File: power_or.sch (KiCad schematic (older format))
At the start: 25 parts

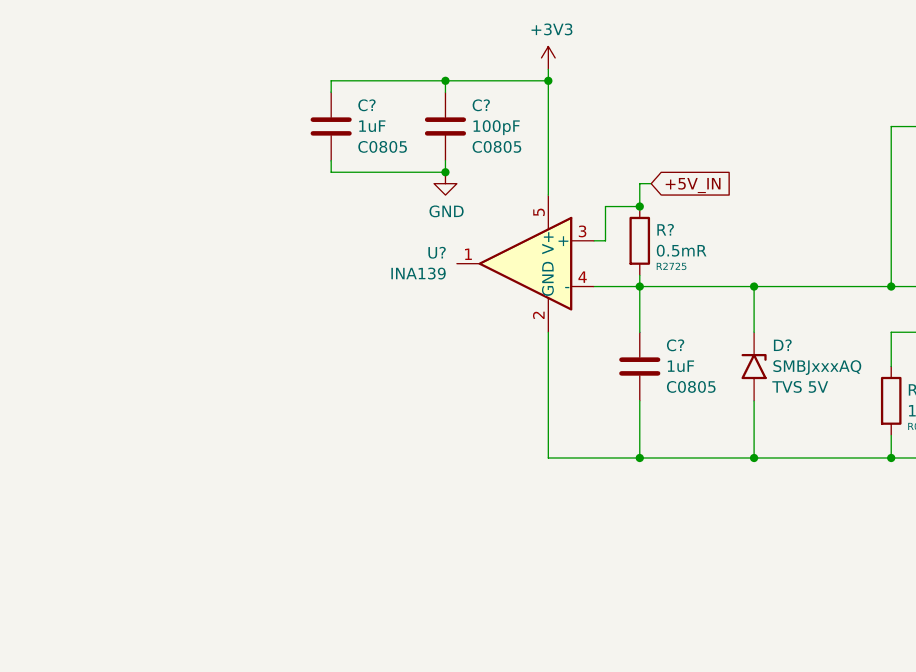
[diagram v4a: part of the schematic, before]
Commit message: move out the current sensor frome power switch
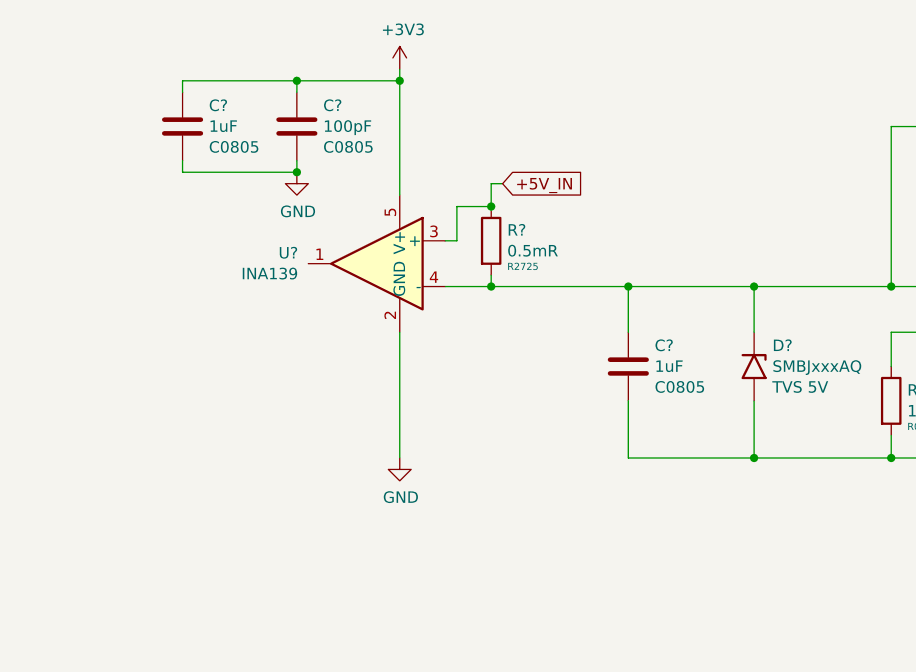
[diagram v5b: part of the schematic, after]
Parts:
- removed C? (x2): 1uF, Capacitor_SMD:C_0805_2012Metric, symbol Device:C
- removed C?: 100pF, Capacitor_SMD:C_0805_2012Metric, symbol Device:C
- removed R?: 0.5mR, Resistor_SMD:R_2725_6865Metric, symbol Device:R
- removed U?: INA139, Package_TO_SOT_SMD:SOT-23-5, symbol Amplifier_Current:INA139
- added C? (x2): 1uF, Capacitor_SMD:C_0805_2012Metric, symbol Device:C
- added C?: 100pF, Capacitor_SMD:C_0805_2012Metric, symbol Device:C
- added R?: 0.5mR, Resistor_SMD:R_2725_6865Metric, symbol Device:R
- added U?: INA139, Package_TO_SOT_SMD:SOT-23-5, symbol Amplifier_Current:INA139
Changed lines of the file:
@@
-$EndComp
-$Comp
-L Amplifier_Current:INA139 U?
-U 1 1 5E3C04AF
-P 6250 1800
-F 0 "U?" H 6594 1846 50  0000 L CNN
-F 1 "INA139" H 6594 1755 50  0000 L CNN
-F 2 "Package_TO_SOT_SMD:SOT-23-5" H 6250 1800 50  0001 C CNN
-F 3 "http://www.ti.com/lit/gpn/ina139" H 6250 1805 50  0001 C CNN
-	1    6250 1800
-	-1   0    0    -1
 $EndComp
 $Comp
@@
 Text GLabel 1400 7300 1    50   Input ~ 0
 +12V_BUS
-Text GLabel 6800 1450 2    50   Input ~ 0
-+5V_IN
 Text GLabel 10600 1750 2    50   Input ~ 0
 +5V_BUS
@@
 	7250 2650 7850 2650
 Connection ~ 7850 2650
-$Comp
-L Device:C C?
-U 1 1 5E3A7B48
-P 6750 2250
-AR Path="/5E350920/5E3A7B48" Ref="C?"  Part="1"
-AR Path="/5E31859C/5E3A7B48" Ref="C?"  Part="1"
-AR Path="/5E3022E2/5E3A7B48" Ref="C?"  Part="1"
-AR Path="/5E3BA3E9/5E3A7B48" Ref="C?"  Part="1"
-F 0 "C?" H 6865 2341 50  0000 L CNN
-F 1 "1uF" H 6865 2250 50  0000 L CNN
-F 2 "Capacitor_SMD:C_0805_2012Metric" H 6788 2100 50  0001 C CNN
-F 3 "~" H 6750 2250 50  0001 C CNN
-F 4 "C0805" H 6865 2159 50  0000 L CNN "size"
-	1    6750 2250
-	1    0    0    -1
-$EndComp
-Wire Wire Line
-	7250 1900 6750 1900
-Wire Wire Line
-	6750 1900 6750 2100
+Wire Wire Line
+	10600 1750 10550 1750
+$Comp
+L Amplifier_Current:INA139 U?
+U 1 1 5E3EB7B6
+P 5600 1800
+F 0 "U?" H 5944 1846 50  0000 L CNN
+F 1 "INA139" H 5944 1755 50  0000 L CNN
+F 2 "Package_TO_SOT_SMD:SOT-23-5" H 5600 1800 50  0001 C CNN
+F 3 "http://www.ti.com/lit/gpn/ina139" H 5600 1805 50  0001 C CNN
+	1    5600 1800
+	-1   0    0    -1
+$EndComp
+Text GLabel 6150 1450 2    50   Input ~ 0
++5V_IN
+$Comp
+L Device:C C?
+U 1 1 5E3EB7BE
+P 6700 2250
+AR Path="/5E350920/5E3EB7BE" Ref="C?"  Part="1"
+AR Path="/5E31859C/5E3EB7BE" Ref="C?"  Part="1"
+AR Path="/5E3022E2/5E3EB7BE" Ref="C?"  Part="1"
+AR Path="/5E3BA3E9/5E3EB7BE" Ref="C?"  Part="1"
+F 0 "C?" H 6815 2341 50  0000 L CNN
+F 1 "1uF" H 6815 2250 50  0000 L CNN
+F 2 "Capacitor_SMD:C_0805_2012Metric" H 6738 2100 50  0001 C CNN
+F 3 "~" H 6700 2250 50  0001 C CNN
+F 4 "C0805" H 6815 2159 50  0000 L CNN "size"
+	1    6700 2250
+	1    0    0    -1
+$EndComp
+Wire Wire Line
+	6700 1900 6700 2100
+Wire Wire Line
+	6700 2400 6700 2650
+$Comp
+L Device:R R?
+U 1 1 5E3EB7C9
+P 6100 1700
+AR Path="/5E300FCE/5E3EB7C9" Ref="R?"  Part="1"
+AR Path="/5E350920/5E3EB7C9" Ref="R?"  Part="1"
+AR Path="/5E3BA3E9/5E3EB7C9" Ref="R?"  Part="1"
+F 0 "R?" H 6170 1746 50  0000 L CNN
+F 1 "0.5mR" H 6170 1655 50  0000 L CNN
+F 2 "Resistor_SMD:R_2725_6865Metric" V 6030 1700 50  0001 C CNN
+F 3 "~" H 6100 1700 50  0001 C CNN
+F 4 "R2725" H 6170 1587 31  0000 L CNN "size"
+	1    6100 1700
+	1    0    0    -1
+$EndComp
+Wire Wire Line
+	6100 1900 6100 1850
+Wire Wire Line
+	5900 1900 6100 1900
+Wire Wire Line
+	5900 1700 5950 1700
+Wire Wire Line
+	5950 1700 5950 1550
+Wire Wire Line
+	5950 1550 6100 1550
+Wire Wire Line
+	5700 2100 5700 2650
+$Comp
+L Device:C C?
+U 1 1 5E3EB7D7
+P 5250 1200
+AR Path="/5E350920/5E3EB7D7" Ref="C?"  Part="1"
+AR Path="/5E31859C/5E3EB7D7" Ref="C?"  Part="1"
+AR Path="/5E3022E2/5E3EB7D7" Ref="C?"  Part="1"
+AR Path="/5E3BA3E9/5E3EB7D7" Ref="C?"  Part="1"
+F 0 "C?" H 5365 1291 50  0000 L CNN
+F 1 "100pF" H 5365 1200 50  0000 L CNN
+F 2 "Capacitor_SMD:C_0805_2012Metric" H 5288 1050 50  0001 C CNN
+F 3 "~" H 5250 1200 50  0001 C CNN
+F 4 "C0805" H 5365 1109 50  0000 L CNN "size"
+	1    5250 1200
+	1    0    0    -1
+$EndComp
+$Comp
+L Device:C C?
+U 1 1 5E3EB7DE
+P 4750 1200
+AR Path="/5E350920/5E3EB7DE" Ref="C?"  Part="1"
+AR Path="/5E31859C/5E3EB7DE" Ref="C?"  Part="1"
+AR Path="/5E3022E2/5E3EB7DE" Ref="C?"  Part="1"
+AR Path="/5E3BA3E9/5E3EB7DE" Ref="C?"  Part="1"
+F 0 "C?" H 4865 1291 50  0000 L CNN
+F 1 "1uF" H 4865 1200 50  0000 L CNN
+F 2 "Capacitor_SMD:C_0805_2012Metric" H 4788 1050 50  0001 C CNN
+F 3 "~" H 4750 1200 50  0001 C CNN
+F 4 "C0805" H 4865 1109 50  0000 L CNN "size"
+	1    4750 1200
+	1    0    0    -1
+$EndComp
+$Comp
+L power:+3V3 #PWR?
+U 1 1 5E3EB7E4
+P 5700 950
+AR Path="/5E300FCE/5E3EB7E4" Ref="#PWR?"  Part="1"
+AR Path="/5E3022E2/5E3EB7E4" Ref="#PWR?"  Part="1"
+AR Path="/5E3BA3E9/5E3EB7E4" Ref="#PWR?"  Part="1"
+F 0 "#PWR?" H 5700 800 50  0001 C CNN
+F 1 "+3V3" H 5715 1123 50  0000 C CNN
+F 2 "" H 5700 950 50  0001 C CNN
+F 3 "" H 5700 950 50  0001 C CNN
+	1    5700 950
+	1    0    0    -1
+$EndComp
+Wire Wire Line
+	5700 950  5700 1000
+$Comp
+L power:GND #PWR?
+U 1 1 5E3EB7EB
+P 5250 1400
+F 0 "#PWR?" H 5250 1150 50  0001 C CNN
+F 1 "GND" H 5255 1227 50  0000 C CNN
+F 2 "" H 5250 1400 50  0001 C CNN
+F 3 "" H 5250 1400 50  0001 C CNN
+	1    5250 1400
+	1    0    0    -1
+$EndComp
+Wire Wire Line
+	4750 1350 4750 1400
+Wire Wire Line
+	4750 1400 5250 1400
+Wire Wire Line
+	5250 1350 5250 1400
+Connection ~ 5250 1400
+Connection ~ 5700 1000
+Wire Wire Line
+	6100 1550 6100 1450
+Connection ~ 6100 1550
+Wire Wire Line
+	6150 1450 6100 1450
+Wire Wire Line
+	4750 1050 4750 1000
+Wire Wire Line
+	4750 1000 5250 1000
+Wire Wire Line
+	5250 1050 5250 1000
+Connection ~ 5250 1000
+Wire Wire Line
+	5250 1000 5700 1000
+Wire Wire Line
+	5700 1000 5700 1500
+Wire Wire Line
+	6700 1900 7250 1900
 Connection ~ 7250 1900
 Wire Wire Line
-	6750 2400 6750 2650
-Wire Wire Line
-	6750 2650 7250 2650
+	7250 2650 6700 2650
 Connection ~ 7250 2650
-$Comp
-L Device:R R?
-U 1 1 5E3B6E0F
-P 6750 1700
-AR Path="/5E300FCE/5E3B6E0F" Ref="R?"  Part="1"
-AR Path="/5E350920/5E3B6E0F" Ref="R?"  Part="1"
-AR Path="/5E3BA3E9/5E3B6E0F" Ref="R?"  Part="1"
-F 0 "R?" H 6820 1746 50  0000 L CNN
-F 1 "0.5mR" H 6820 1655 50  0000 L CNN
-F 2 "Resistor_SMD:R_2725_6865Metric" V 6680 1700 50  0001 C CNN
-F 3 "~" H 6750 1700 50  0001 C CNN
-F 4 "R2725" H 6820 1587 31  0000 L CNN "size"
-	1    6750 1700
-	1    0    0    -1
-$EndComp
-Wire Wire Line
-	6750 1900 6750 1850
-Connection ~ 6750 1900
-Wire Wire Line
-	6550 1900 6750 1900
-Wire Wire Line
-	6550 1700 6600 1700
-Wire Wire Line
-	6600 1700 6600 1550
-Wire Wire Line
-	6600 1550 6750 1550
-Wire Wire Line
-	6350 2100 6350 2650
-Wire Wire Line
-	6350 2650 6750 2650
-Connection ~ 6750 2650
-$Comp
-L Device:C C?
-U 1 1 5E3BFE86
-P 5900 1200
-AR Path="/5E350920/5E3BFE86" Ref="C?"  Part="1"
-AR Path="/5E31859C/5E3BFE86" Ref="C?"  Part="1"
-AR Path="/5E3022E2/5E3BFE86" Ref="C?"  Part="1"
-AR Path="/5E3BA3E9/5E3BFE86" Ref="C?"  Part="1"
-F 0 "C?" H 6015 1291 50  0000 L CNN
-F 1 "100pF" H 6015 1200 50  0000 L CNN
-F 2 "Capacitor_SMD:C_0805_2012Metric" H 5938 1050 50  0001 C CNN
-F 3 "~" H 5900 1200 50  0001 C CNN
-F 4 "C0805" H 6015 1109 50  0000 L CNN "size"
-	1    5900 1200
-	1    0    0    -1
-$EndComp
-$Comp
-L Device:C C?
-U 1 1 5E3BFE90
-P 5400 1200
-AR Path="/5E350920/5E3BFE90" Ref="C?"  Part="1"
-AR Path="/5E31859C/5E3BFE90" Ref="C?"  Part="1"
-AR Path="/5E3022E2/5E3BFE90" Ref="C?"  Part="1"
-AR Path="/5E3BA3E9/5E3BFE90" Ref="C?"  Part="1"
-F 0 "C?" H 5515 1291 50  0000 L CNN
-F 1 "1uF" H 5515 1200 50  0000 L CNN
-F 2 "Capacitor_SMD:C_0805_2012Metric" H 5438 1050 50  0001 C CNN
-F 3 "~" H 5400 1200 50  0001 C CNN
-F 4 "C0805" H 5515 1109 50  0000 L CNN "size"
-	1    5400 1200
-	1    0    0    -1
-$EndComp
-$Comp
-L power:+3V3 #PWR?
-U 1 1 5E3C8024
-P 6350 950
-AR Path="/5E300FCE/5E3C8024" Ref="#PWR?"  Part="1"
-AR Path="/5E3022E2/5E3C8024" Ref="#PWR?"  Part="1"
-AR Path="/5E3BA3E9/5E3C8024" Ref="#PWR?"  Part="1"
-F 0 "#PWR?" H 6350 800 50  0001 C CNN
-F 1 "+3V3" H 6365 1123 50  0000 C CNN
-F 2 "" H 6350 950 50  0001 C CNN
-F 3 "" H 6350 950 50  0001 C CNN
-	1    6350 950
-	1    0    0    -1
-$EndComp
-Wire Wire Line
-	6350 950  6350 1000
+Connection ~ 6100 1900
+Wire Wire Line
+	6100 1900 6700 1900
+Connection ~ 6700 1900
 $Comp
 L power:GND #PWR?
-U 1 1 5E3CF282
-P 5900 1400
-F 0 "#PWR?" H 5900 1150 50  0001 C CNN
-F 1 "GND" H 5905 1227 50  0000 C CNN
-F 2 "" H 5900 1400 50  0001 C CNN
-F 3 "" H 5900 1400 50  0001 C CNN
-	1    5900 1400
-	1    0    0    -1
-$EndComp
-Wire Wire Line
-	5400 1350 5400 1400
-Wire Wire Line
-	5400 1400 5900 1400
-Wire Wire Line
-	5900 1350 5900 1400
-Connection ~ 5900 1400
-Connection ~ 6350 1000
-Wire Wire Line
-	6750 1550 6750 1450
-Connection ~ 6750 1550
-Wire Wire Line
-	6800 1450 6750 1450
-Wire Wire Line
-	10600 1750 10550 1750
-Wire Wire Line
-	5400 1050 5400 1000
-Wire Wire Line
-	5400 1000 5900 1000
-Wire Wire Line
-	5900 1050 5900 1000
-Connection ~ 5900 1000
-Wire Wire Line
-	5900 1000 6350 1000
-Wire Wire Line
-	6350 1000 6350 1500
+U 1 1 5E405553
+P 5700 2650
+F 0 "#PWR?" H 5700 2400 50  0001 C CNN
+F 1 "GND" H 5705 2477 50  0000 C CNN
+F 2 "" H 5700 2650 50  0001 C CNN
+F 3 "" H 5700 2650 50  0001 C CNN
+	1    5700 2650
+	1    0    0    -1
+$EndComp
 $EndSCHEMATC

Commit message: currentsensor v1
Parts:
- removed Q?: PSMN1R8-40YLC, Package_TO_SOT_SMD:LFPAK56, symbol Transistor_FET:PSMN1R8-40YLC
- added C?: 2.2uF, Capacitor_SMD:C_1206_3216Metric, symbol Device:C
- added C? (x3): 100pF, Capacitor_SMD:C_0805_2012Metric, symbol Device:C
- added C? (x3): 1uF, Capacitor_SMD:C_0805_2012Metric, symbol Device:C
- added D? (x2): SMBJxxxAQ, Diode_SMD:D_SMB, symbol Diode:SMBJxxxAQ
- added Q? (x3): 2N7002, Package_TO_SOT_SMD:SOT-23, symbol Transistor_FET:2N7002
- added Q?: PSMN1R8-40YLC, Package_TO_SOT_SMD:LFPAK56, symbol Transistor_FET:PSMN1R8-40YLC
- added R? (x5): 10K, Resistor_SMD:R_0805_2012Metric, symbol Device:R
- added R? (x2): 100K, Resistor_SMD:R_0805_2012Metric, symbol Device:R
- added R?: 100R, Resistor_SMD:R_0805_2012Metric, symbol Device:R
- added R?: 0.5mR, Resistor_SMD:R_2725_6865Metric, symbol Device:R
- added U?: LM5050-1, Package_TO_SOT_SMD:TSOT-23-6, symbol Power_Management:LM5050-1
- added U?: INA139, Package_TO_SOT_SMD:SOT-23-5, symbol Amplifier_Current:INA139
- R?: value 4.7K -> 10K
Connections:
- net labels added: CurentSensor5V_100X, CurentSensor5V_10X
- net labels removed: ?
- wire segments 93 -> 185
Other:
- moved on the sheet: C?, D?, Q?, R?, U?

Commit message: power or switch v1
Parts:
- added Q?: PSMN1R8-40YLC, Package_TO_SOT_SMD:LFPAK56, symbol Transistor_FET:PSMN1R8-40YLC
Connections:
- net labels added: CurentSensor12V, CurentSensor12V_Scale_100X, CurentSensor12V_Scale_10X, CurentSensor5V, CurentSensor5V_Scale_100X, CurentSensor5V_Scale_10X, Enable_12V, Enable_5V
- net labels removed: CurentSensor5V_100X, CurentSensor5V_10X
- wire segments 185 -> 197
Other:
- moved on the sheet: C?, D?, Q?, R?, U?
